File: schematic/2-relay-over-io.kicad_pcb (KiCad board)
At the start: 2 copper layers, 86.4 x 51.4 mm, 26 parts, among them J1 WJ142R-5.08-3P, J2 WJ142R-5.08-3P, J5 Conn_02x05_Odd_Even, J6 Conn_02x05_Odd_Even, J7 Conn_02x08_Odd_Even, J8 Conn_02x08_Odd_Even, Q2 BC817, Q3 BC817, U1 SONGLE_3V_relay, U2 SONGLE_3V_relay, U6 DizzyBITLogo, U7 DizzyBIT-Layout

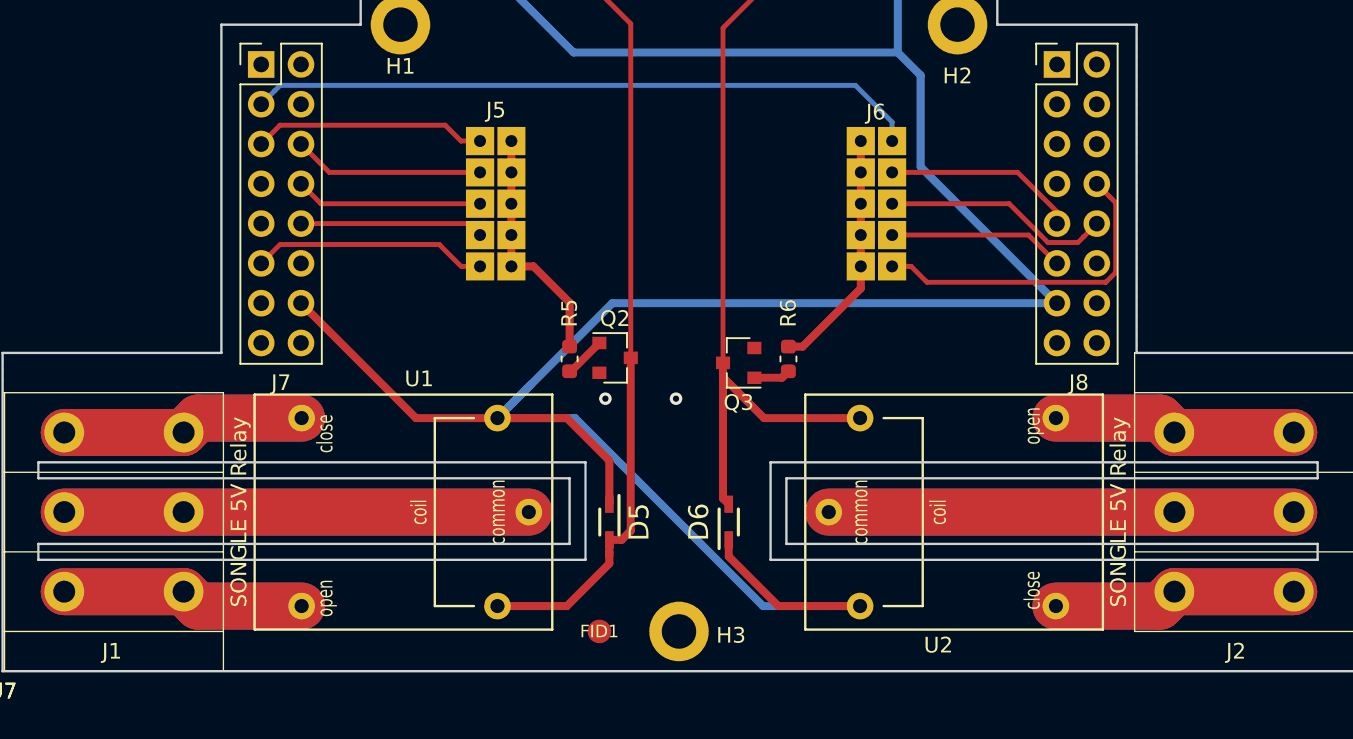
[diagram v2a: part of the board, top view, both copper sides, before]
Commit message: Changed Connector designators
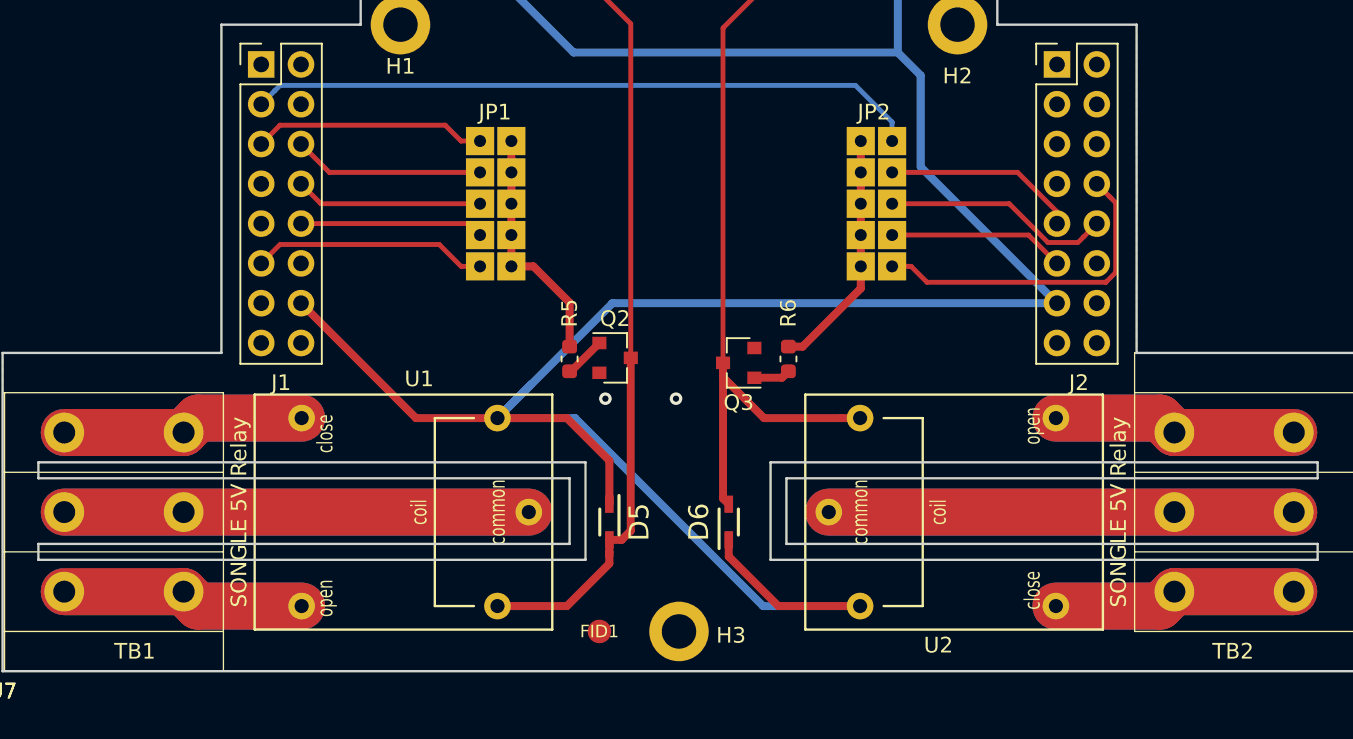
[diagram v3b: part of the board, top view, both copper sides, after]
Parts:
- removed J5, J6: Conn_02x05_Odd_Even, DizzyBit:DizzyBit-SolderJumper-5-5-Open
- removed J7, J8: Conn_02x08_Odd_Even, Connector_PinHeader_2.54mm:PinHeader_2x08_P2.54mm_Vertical
- added JP1: Conn_02x05_Odd_Even, DizzyBit:DizzyBit-SolderJumper-5-5-Open, F.Cu at (105.7, 111.2)
- added JP2: Conn_02x05_Odd_Even, DizzyBit:DizzyBit-SolderJumper-5-5-Open, F.Cu at (134.0, 121.2)
- added TB1: WJ142R-5.08-3P, TerminalBlock:WJ142R-5.08-3P, F.Cu at (90.3, 146.1)
- added TB2: WJ142R-5.08-3P, TerminalBlock:WJ142R-5.08-3P, F.Cu at (148.5, 125.7)
- J1, J2: value WJ142R-5.08-3P -> Conn_02x08_Odd_Even; footprint TerminalBlock:WJ142R-5.08-3P -> Connector_PinHeader_2.54mm:PinHeader_2x08_P2.54mm_Vertical
- moved J1 38.8 mm to (92.7, 107.3), turned to 0 degrees
- moved J2 19.1 mm to (143.5, 107.3)
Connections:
- J1 pad 1: Net-(J1-Pad1) -> I39
- J1 pad 2: Net-(J1-Pad2) -> I36
- J1 pad 3: Net-(J1-Pad3) -> IO33
- J2 pad 1: Net-(J2-Pad1) -> VSPI_MOSI
- J2 pad 2: Net-(J2-Pad2) -> I2C_SCL
- J2 pad 3: Net-(J2-Pad3) -> IO1
- U1 pad 3: Net-(J1-Pad2) -> Net-(TB1-Pad2)
- U1 pad 4: Net-(J1-Pad3) -> Net-(TB1-Pad3)
- U1 pad 5: Net-(J1-Pad1) -> Net-(TB1-Pad1)
- U2 pad 3: Net-(J2-Pad2) -> Net-(TB2-Pad2)
- U2 pad 4: Net-(J2-Pad3) -> Net-(TB2-Pad3)
- U2 pad 5: Net-(J2-Pad1) -> Net-(TB2-Pad1)
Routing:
- net Net-(TB2-Pad2): track 0.00 -> 59.4 mm
- net Net-(J2-Pad2): track 59.4 -> 0.00 mm
- net Net-(TB1-Pad2): track 0.00 -> 59.3 mm
- net Net-(J1-Pad2): track 59.3 -> 0.00 mm
- net Net-(TB2-Pad1): track 0.00 -> 31.1 mm
- net Net-(J2-Pad1): track 31.1 -> 0.00 mm
- net Net-(TB2-Pad3): track 0.00 -> 31.1 mm
- net Net-(J2-Pad3): track 31.1 -> 0.00 mm
- net Net-(TB1-Pad3): track 0.00 -> 31.1 mm
- net Net-(J1-Pad3): track 31.1 -> 0.00 mm
- net Net-(TB1-Pad1): track 0.00 -> 31.1 mm
- net Net-(J1-Pad1): track 31.1 -> 0.00 mm
